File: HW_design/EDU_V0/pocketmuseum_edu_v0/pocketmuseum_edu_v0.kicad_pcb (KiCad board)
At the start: 4 copper layers, 89 x 51 mm, 141 parts, among them J101 USB_C_Receptacle_USB2.0_16P, J201 DM3AT-SF-PEJM5, J202 1x6P 2.54mm SMD, J203 1x6P 2.54mm SMD, J204 BM04B-SRSS-TB, J205 BM04B-SRSS-TB, J206 BM04B-SRSS-TB, J401 PJ31060-I, J402 PJ31060-I, Q201 L8050QLT1G, Q202 L8050QLT1G, Q401 BSS138LT3G, Q402 BSS138LT3G, SW201 PTS636, SW202 PTS636, U101 AMS1117-3.3, U102 AMS1117-3.3, U201 ESP32-C6-MINI-1/U, U301 LSM6DSL, U302 ICP20100, U401 ES8388

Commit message: Updated Readme
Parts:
- removed C103, C104: 22u, Capacitor_SMD:C_0603_1608Metric
- removed C306, C418, C420, C422: 1u, Capacitor_SMD:C_0402_1005Metric
- removed C307, C308, C411, C415, C416, C417, C419, C421: 0u1, Capacitor_SMD:C_0402_1005Metric
- removed C410, C412, C423: 10u, Capacitor_SMD:C_0603_1608Metric
- removed C413, C414: 20p, Capacitor_SMD:C_0402_1005Metric
- removed C424, C425: 47u, Capacitor_SMD:C_0603_1608Metric
- removed D202, D203, D204, D205: LESD5D5.0CT1G, Diode_SMD:D_SOD-523
- removed D301, D302, D303, D304, D305, D306: SK6805-EC20, SK_RGB:SK68xx-EC20
- removed J202, J203: 1x6P 2.54mm SMD, Connector_PinHeader_2.54mm:PinHeader_1x06_P2.54mm_Vertical_SMD_Pin1Right
- removed J204: BM04B-SRSS-TB, Connector_JST:JST_SH_BM04B-SRSS-TB_1x04-1MP_P1.00mm_Vertical
- removed J401, J402: PJ31060-I, Connector_Audio:Jack_3.5mm_PJ31060-I_Horizontal
- removed Q201, Q202: L8050QLT1G, Package_TO_SOT_SMD:SOT-23
- removed Q401, Q402: BSS138LT3G, Package_TO_SOT_SMD:SOT-23
- removed R105, R416, R417: 10R, Resistor_SMD:R_0603_1608Metric
- removed the R206 at (180.9, 80.6)
- removed R216, R217, R218, R219, R221, R418, R419, R420: 0R, Resistor_SMD:R_0603_1608Metric
- removed R401, R409, R410: 100R, Resistor_SMD:R_0402_1005Metric
- removed R402, R411, R415: 2k, Resistor_SMD:R_0402_1005Metric
- removed R403: 4R7, Resistor_SMD:R_0402_1005Metric
- removed R404, R405, R406, R407, R408: 33R, Resistor_SMD:R_0402_1005Metric
- removed R412: 100k, Resistor_SMD:R_0402_1005Metric
- removed R413, R414, R421, R422: 1k, Resistor_SMD:R_0402_1005Metric
- removed R423, R424: 10k, Resistor_SMD:R_0402_1005Metric
- removed SW202: PTS636, Button_Switch_SMD:SW_Tactile_SPST_NO_Straight_CK_PTS636Sx25SMTRLFS
- removed U101: AMS1117-3.3, Package_TO_SOT_SMD:SOT-223-3_TabPin2
- removed U401: ES8388, Package_DFN_QFN:QFN-28-1EP_4x4mm_P0.45mm_EP2.6x2.6mm
- added D2: LESD5D5.0CT1G, Diode_SMD:D_SOD-523, F.Cu at (110.0, 169.7)
- added D4: LESD5D5.0CT1G, Diode_SMD:D_SOD-523, F.Cu at (110.0, 172.2)
- added D401: SK6805-EC20, SK_RGB:SK68xx-EC20, B.Cu at (166.1, 104.8)
- added D402: SK6805-EC20, SK_RGB:SK68xx-EC20, B.Cu at (150.8, 104.8)
- added D403: SK6805-EC20, SK_RGB:SK68xx-EC20, B.Cu at (135.3, 104.6)
- added D404: SK6805-EC20, SK_RGB:SK68xx-EC20, B.Cu at (180.8, 104.8)
- added D405: SK6805-EC20, SK_RGB:SK68xx-EC20, B.Cu at (166.2, 90.0)
- added D406: SK6805-EC20, SK_RGB:SK68xx-EC20, B.Cu at (150.8, 89.8)
- added D407: SK6805-EC20, SK_RGB:SK68xx-EC20, B.Cu at (127.7, 78.0)
- added D408: SK6805-EC20, SK_RGB:SK68xx-EC20, B.Cu at (127.7, 91.8)
- added D409: SK6805-EC20, SK_RGB:SK68xx-EC20, B.Cu at (114.0, 91.8)
- added J102: JST PH S2B, Connector_JST:JST_PH_S2B-PH-SM4-TB_1x02-1MP_P2.00mm_Horizontal, F.Cu at (135.8, 76.8)
- added Q301: BSS138, Package_TO_SOT_SMD:SOT-23, F.Cu at (81.0, 99.8)
- added Q302: BSS138, Package_TO_SOT_SMD:SOT-23, F.Cu at (81.0, 104.4)
- added Q303: BSS138, Package_TO_SOT_SMD:SOT-23, F.Cu at (81.0, 109.0)
- added R303: 4k7, Resistor_SMD:R_0603_1608Metric, F.Cu at (99.9, 150.6)
- added R304: 4k7, Resistor_SMD:R_0603_1608Metric, F.Cu at (99.9, 153.1)
- added R305: 10k, Resistor_SMD:R_0603_1608Metric, F.Cu at (99.9, 155.6)
- added R306: 0R, Resistor_SMD:R_0603_1608Metric, F.Cu at (99.9, 158.1)
- added R307: 0R, Resistor_SMD:R_0603_1608Metric, F.Cu at (99.9, 160.6)
- added SW1: SW_SPDT, Button_Switch_SMD:SW_SPDT_PCM12, F.Cu at (123.5, 67.6)
- added U1: TLV740P18, Package_TO_SOT_SMD:SOT-23-5, F.Cu at (93.4, 133.8)
- added U302: ICP20100, Package_LGA:ST_HLGA-10_2x2mm_P0.5mm_LayoutBorder3x2y, F.Cu at (103.8, 160.0)
- C204: moved to F.Cu
- C301, C302, C303, C304, C305: value 1u -> 0u1; moved to F.Cu
- C401, C403, C405, C408: value 10u -> 1u; footprint Capacitor_SMD:C_0603_1608Metric -> Capacitor_SMD:C_0402_1005Metric
- C402, C404, C406, C407, C409: value 0u1 -> 1u
- D201: value LESD5D5.0CT1G -> LED; footprint Diode_SMD:D_SOD-523 -> LED_SMD:LED_0402_1005Metric
- J201: value DM3AT-SF-PEJM5 -> TF-015; footprint Connector_Card:microSD_HC_Hirose_DM3AT-SF-PEJM5 -> microSD:TF-015_SOFNG
- J205, J206: footprint Connector_JST:JST_SH_BM04B-SRSS-TB_1x04-1MP_P1.00mm_Vertical -> Connector_JST:JST_SH_SM04B-SRSS-TB_1x04-1MP_P1.00mm_Horizontal
- R208: value 10k -> 0R; footprint Resistor_SMD:R_0402_1005Metric -> Resistor_SMD:R_0603_1608Metric
- R214: value 0R -> 10k; footprint Resistor_SMD:R_0603_1608Metric -> Resistor_SMD:R_0402_1005Metric
- R215: value 0R -> 2k; footprint Resistor_SMD:R_0603_1608Metric -> Resistor_SMD:R_0402_1005Metric
- R301, R302: value 0R -> 10k; moved to F.Cu
- R303, R304: value 0R -> 4k7
- U301: value LSM6DSL -> ICM-20948; footprint Package_LGA:LGA-14_3x2.5mm_P0.5mm_LayoutBorder3x4y -> Sensor_Motion:InvenSense_QFN-24_3x3mm_P0.4mm
- moved D102 111.6 mm to (202.0, 149.3)
- moved D101 111.6 mm to (202.0, 143.0)
- moved R102 111.6 mm to (196.5, 140.3)
- moved R101 111.6 mm to (196.5, 151.9)
- moved C304 85.3 mm to (108.3, 151.2)
- moved C303 84.0 mm to (108.3, 149.2), turned to 0 degrees
- moved C401 73.4 mm to (76.8, 137.4), turned to 0 degrees
- moved C402 72.6 mm to (76.8, 139.3), turned to 0 degrees
- moved C305 72.2 mm to (108.3, 153.2)
- moved C403 69.6 mm to (76.8, 141.3)
- moved R302 68.9 mm to (99.9, 148.1), turned to 0 degrees
- moved C408 68.6 mm to (82.5, 139.3), turned to 0 degrees
- moved R301 68.6 mm to (99.9, 145.6)
- moved J101 67.6 mm to (165.6, 112.7), turned to 0 degrees
- moved C302 66.8 mm to (108.3, 147.2), turned to 0 degrees
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- renumbered R207 to R206, R220 to R207
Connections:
- net Net-(J101-CC1) renamed /Power/USB_CC1
- net Net-(J101-CC2) renamed /Power/USB_CC2
- C204 pad 1: /MCU/CHIP_PU -> GND
- C204 pad 2: GND -> /MCU/CHIP_PU
- C301 pad 1: GND -> +1.8V
- C301 pad 2: +3.3V -> GND
- C302 pad 2: +3.3V -> +1.8V
- C303 pad 2: +3.3V -> Net-(U301-REGOUT)
- C304 pad 1: GND -> +3.3V
- C304 pad 2: +3.3V -> GND
- C401 pad 1: +3.3V -> GND
- C401 pad 2: GND -> +3.3V
- C402 pad 1: /Audio CODEC/ES8388_DVDD -> GND
- C402 pad 2: GND -> +3.3V
- C403 pad 1: +3.3VA -> GND
- C403 pad 2: GND -> +3.3V
- C404 pad 1: +3.3VA -> GND
- C404 pad 2: GND -> +3.3V
- C405 pad 1: /Audio CODEC/ES8388_AVDD -> GND
- C405 pad 2: GND -> +3.3V
- C406 pad 1: /Audio CODEC/ES8388_AVDD -> GND
- C406 pad 2: GND -> +3.3V
- C407 pad 1: /Audio CODEC/ES8388_VREF -> GND
- C407 pad 2: GND -> +3.3V
- C408 pad 1: /Audio CODEC/ES8388_VREF -> GND
- C408 pad 2: GND -> +3.3V
- C409 pad 1: /Audio CODEC/ES8388_ADCVREF -> GND
- C409 pad 2: GND -> +3.3V
- D201 pad 2: /MCU/FTDI_DTR -> Net-(D201-A)
- J101 pad A6: unconnected-(J101-D+-PadA6) -> USB_D+
- J101 pad A7: unconnected-(J101-D--PadA7) -> USB_D-
- J101 pad B6: unconnected-(J101-D+-PadB6) -> USB_D+
- J101 pad B7: unconnected-(J101-D--PadB7) -> USB_D-
- J101 pad S1: /Power/USB_shield_disconnect -> unconnected-(J101-SHIELD-PadS1)_2
- J201 pad 1: /MCU/uSD_DAT2 -> /MCU/SD_DAT2
- J201 pad 10: /MCU/SD_DETECT -> /MCU/SD_Shield_Diconnect
- J201 pad 2: /MCU/uSD_DAT3 -> /MCU/SPI_CS
- J201 pad 3: /MCU/uSD_CMD -> /MCU/SPI_MOSI
- J201 pad 5: /MCU/uSD_CLK -> /MCU/SPI_SCK
- J201 pad 7: /MCU/uSD_DAT0 -> /MCU/SPI_MISO
- J201 pad 8: /MCU/uSD_DAT1 -> /MCU/SD_DAT1
- J201 pad 9: +3.3V -> /MCU/SD_DETECT
- J205 pad MP: unconnected-(J205-MountPin-PadMP)_1 -> /MCU/unconnected-(J205-MountPin-PadMP)_1
- J206 pad 2: /MCU/STRAP_GPIO8 -> /MCU/CHIP_PU
- J206 pad 3: /MCU/SD_DETECT -> /MCU/UART0_RX
- J206 pad 4: /MCU/MCU_GPIO14 -> /MCU/UART0_TX
- J206 pad MP: unconnected-(J206-MountPin-PadMP) -> /MCU/unconnected-(J206-MountPin-PadMP)_1_1
- R205 pad 1: /MCU/FTDI_DTR -> +3.3V
- R205 pad 2: /MCU/DTR -> /MCU/STRAP_GPIO_9
- R207 pad 2: GND -> +3.3V
- R208 pad 1: /MCU/uSD_DAT1 -> /MCU/SD_Shield_Diconnect
- R208 pad 2: +3.3V -> GND
- R209 pad 1: /MCU/uSD_DAT0 -> /MCU/SPI_MISO
- R210 pad 1: /MCU/uSD_CLK -> /MCU/SPI_SCK
- R211 pad 1: /MCU/uSD_CMD -> /MCU/SPI_MOSI
- R212 pad 1: /MCU/uSD_DAT3 -> /MCU/SPI_CS
- R213 pad 1: /MCU/uSD_DAT2 -> /MCU/SD_DAT1
- R214 pad 1: /MCU/uSD_DAT2 -> /MCU/SD_DAT2
- R214 pad 2: /MCU/SDIO_DAT2 -> +3.3V
- R215 pad 1: /MCU/uSD_DAT3 -> /MCU/DBG_LED
- R215 pad 2: /MCU/SDIO_DAT3 -> Net-(D201-A)
- R301 pad 1: Net-(U301-SDA) -> +1.8V
- R301 pad 2: I2C_SDA -> /Sensors/ICM20x_SCL
- R302 pad 1: Net-(U301-SCL) -> +1.8V
- R302 pad 2: I2C_SCL -> /Sensors/ICM20x_SDA
- R303 pad 1: Net-(U302-SCL) -> +3.3V
- R304 pad 1: Net-(U302-SDA) -> +1.8V
- R304 pad 2: I2C_SDA -> /Sensors/ICM20x_INT
- U201 pad 10: /MCU/STRAP_MTDI -> unconnected-(U201-MTDI/GPIO5/ADC1_CH5-Pad10)
- U201 pad 12: I2S_DOUT -> unconnected-(U201-GPIO0/ADC1_CH0/XTAL_32K_P-Pad12)
- U201 pad 13: I2S_LRCK -> unconnected-(U201-GPIO1/ADC1_CH1/XTAL_32K_N-Pad13)
- U201 pad 15: I2S_DIN -> unconnected-(U201-MTCK/GPIO6/ADC1_CH6-Pad15)
- U201 pad 16: I2S_BCK -> /MCU/DBG_LED
- U201 pad 17: I2S_MCLK -> USB_D-
- U201 pad 18: AUX_IN_DETECT -> USB_D+
- U201 pad 19: /MCU/MCU_GPIO14 -> unconnected-(U201-GPIO14-Pad19)
- U201 pad 24: /MCU/SDIO_CMD -> /MCU/SPI_MOSI
- U201 pad 25: /MCU/SDIO_CLK -> /MCU/SPI_SCK
- U201 pad 26: /MCU/SDIO_DAT0 -> /MCU/SPI_MISO
- U201 pad 27: /MCU/SDIO_DAT1 -> unconnected-(U201-GPIO21-Pad27)
- U201 pad 28: /MCU/SDIO_DAT2 -> unconnected-(U201-GPIO22-Pad28)
- U201 pad 29: /MCU/SDIO_DAT3 -> /MCU/SPI_CS
- U201 pad 9: /MCU/STRAP_MTMS -> unconnected-(U201-MTMS/GPIO4/ADC1_CH4-Pad9)
- U301 pad 1: GND -> unconnected-(U301-NC-Pad1)
- U301 pad 10: unconnected-(U301-NC-Pad10) -> Net-(U301-REGOUT)
- U301 pad 12: +3.3V -> /Sensors/ICM20x_INT
- U301 pad 13: Net-(U301-SCL) -> +1.8V
- U301 pad 14: Net-(U301-SDA) -> unconnected-(U301-NC-Pad14)
- U301 pad 2: GND -> unconnected-(U301-NC-Pad2)
- U301 pad 3: GND -> unconnected-(U301-NC-Pad3)
- U301 pad 5: +3.3V -> unconnected-(U301-NC-Pad5)
- U301 pad 6: GND -> unconnected-(U301-NC-Pad6)
- U301 pad 7: GND -> unconnected-(U301-AUX_CL-Pad7)
- U301 pad 8: +3.3V -> +1.8V
- U301 pad 9: unconnected-(U301-INT2-Pad9) -> GND
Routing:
- net +3.3V: track 287.9 -> 0.00 mm, vias 13 -> 0
- net GND: track 115.8 -> 0.00 mm, vias 142 -> 0
- net VBUS: track 103.4 -> 0.00 mm, vias 2 -> 0
- net I2C_SCL: track 82.4 -> 0.00 mm, vias 1 -> 0
- net I2C_SDA: track 65.7 -> 0.00 mm, vias 1 -> 0
- net /Audio CODEC/AUX_Det: track 60.7 -> 0.00 mm
- net /MCU/SD_DETECT: track 52.4 -> 0.00 mm
- net +3.3VA: track 44.6 -> 0.00 mm
- net AUX_IN_DETECT: track 41.2 -> 0.00 mm
- net ES8388_I2S_MCLK: track 40.0 -> 0.00 mm
- net ES8388_I2S_BCK: track 34.3 -> 0.00 mm
- net ES8388_I2S_DIN: track 32.3 -> 0.00 mm
- net ES8388_I2S_LRCK: track 30.3 -> 0.00 mm
- net I2S_DOUT: track 28.6 -> 0.00 mm
- net /MCU/CHIP_PU: track 27.9 -> 0.00 mm, vias 2 -> 0
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- removed copper zone on B.Cu, net +3.3V
- removed copper zone on F.Cu, net +3.3V
- removed copper zone on F.Cu, net +3.3VA
- removed copper zone on F.Cu, net +5V
- removed copper zone on F.Cu, net /Audio CODEC/AUX_VREF
- removed copper zone on F.Cu, net /Audio CODEC/ES8388_DVDD
- removed copper zone on F.Cu, net /MCU/CHIP_PU
- removed copper zone on F.Cu, net /Power/5V_Filt_A
- removed copper zone on F.Cu, net /Power/5V_Filt_D
- removed copper zone on B.Cu, net GND
- removed copper zone on F.Cu, net GND
- removed copper zone on In1.Cu, net GND
- removed copper zone on In2.Cu, net GND
- removed copper zone on F.Cu, net VBUS
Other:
- board size 89 x 51 mm -> 92.1 x 51 mm
- board text removed: "14"
- board text removed: "9"
- board text removed: "AUX IN"
- board text removed: "BARO."
- board text removed: "FTDI"
- board text removed: "GPIO"
- board text removed: "I2C"
- board text removed: "I2S"
- board text removed: "IMU"
- board text removed: "MTx & VA"
- board text removed: "PHONES OUT"
- board text removed: "PWR IN"
- board text removed: "SD CARD"
- board text removed: "SOUNCARD DEV. V0"
- board text removed: "_2_"
- board text removed: "_3_"
- board text removed: "_4_"
- board text removed: "_5_"
- board text removed: "_gpio9"
- board text removed: "_reset"

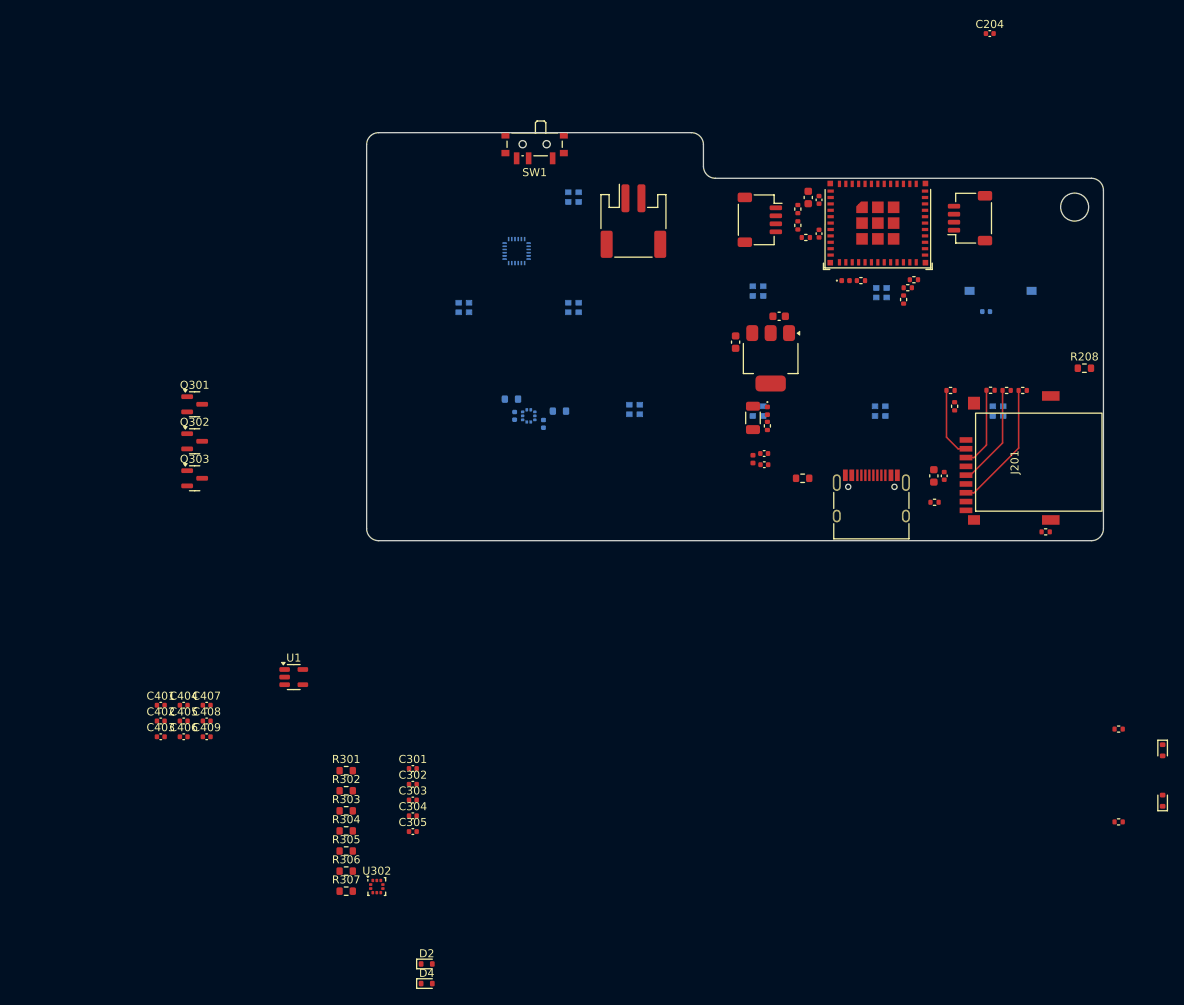
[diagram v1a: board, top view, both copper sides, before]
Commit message: Added Mic & Light Sensor to EDU_V0
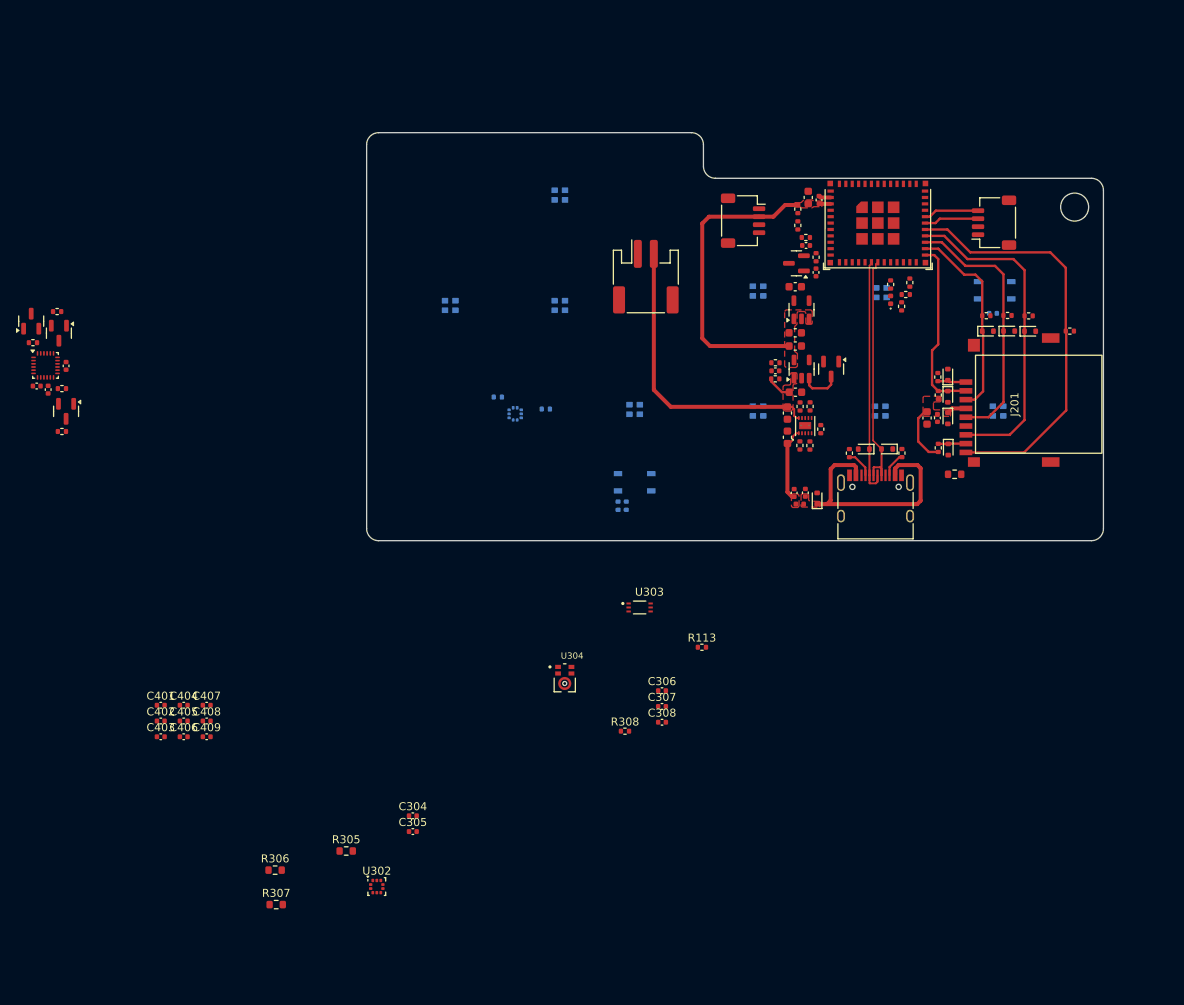
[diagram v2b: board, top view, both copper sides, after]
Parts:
- removed the C106 at (154.1, 88.8)
- removed C205: 1u, Capacitor_SMD:C_0402_1005Metric
- removed C309, C310: 0u1, Capacitor_SMD:C_0402_1005Metric
- removed D2, D4: LESD5D5.0CT1G, Diode_SMD:D_SOD-523
- removed SW1: SW_SPDT, Button_Switch_SMD:SW_SPDT_PCM12
- removed U1: TLV740P18, Package_TO_SOT_SMD:SOT-23-5
- added C103: 10u, Capacitor_SMD:C_0603_1608Metric, F.Cu at (155.1, 103.9)
- added C104: 10u, Capacitor_SMD:C_0603_1608Metric, F.Cu at (155.1, 100.8)
- added C105: 1u, Capacitor_SMD:C_0402_1005Metric, F.Cu at (153.6, 95.6)
- added C107: 10u, Capacitor_SMD:C_0603_1608Metric, F.Cu at (156.1, 98.2)
- added C108: 10u, Capacitor_SMD:C_0603_1608Metric, F.Cu at (156.1, 92.5)
- added C109: 10u, Capacitor_SMD:C_0603_1608Metric, F.Cu at (156.1, 90.8)
- added C110: 10u, Capacitor_SMD:C_0603_1608Metric, F.Cu at (156.1, 85.1)
- added C306: 0u1, Capacitor_SMD:C_0402_1005Metric, F.Cu at (139.4, 135.6)
- added C307: 1u, Capacitor_SMD:C_0402_1005Metric, F.Cu at (139.4, 137.5)
- added C308: 0u1, Capacitor_SMD:C_0402_1005Metric, F.Cu at (139.4, 139.5)
- added D104: BAT54C, Package_TO_SOT_SMD:SOT-23, F.Cu at (160.6, 95.3)
- added D202: LESD5D5.0CT1G, Diode_SMD:D_SOD-523, F.Cu at (185.4, 90.6)
- added D203: LESD5D5.0CT1G, Diode_SMD:D_SOD-523, F.Cu at (182.8, 90.6)
- added D204: LESD5D5.0CT1G, Diode_SMD:D_SOD-523, F.Cu at (175.2, 101.5)
- added D205: LESD5D5.0CT1G, Diode_SMD:D_SOD-523, F.Cu at (180.2, 90.6)
- added D206: LESD5D5.0CT1G, Diode_SMD:D_SOD-523, F.Cu at (175.2, 98.8)
- added D207: LESD5D5.0CT1G, Diode_SMD:D_SOD-523, F.Cu at (175.2, 96.0)
- added D208: LED, LED_SMD:LED_0402_1005Metric, F.Cu at (168.0, 86.7)
- added R105: 10k, Resistor_SMD:R_0402_1005Metric, F.Cu at (156.7, 100.0)
- added R107: 10k, Resistor_SMD:R_0402_1005Metric, F.Cu at (159.3, 102.9)
- added R108: 61k9, Resistor_SMD:R_0402_1005Metric, F.Cu at (153.6, 94.6)
- added R109: 178k, Resistor_SMD:R_0402_1005Metric, F.Cu at (153.6, 96.6)
- added R110: 100k, Resistor_SMD:R_0402_1005Metric, F.Cu at (158.7, 81.4)
- added R111: 2k7, Resistor_SMD:R_0402_1005Metric, B.Cu at (133.9, 112.4)
- added R112: 10k, Resistor_SMD:R_0402_1005Metric, B.Cu at (134.9, 112.4)
- added R113: 10k, Resistor_SMD:R_0402_1005Metric, F.Cu at (144.4, 130.1)
- added R308: 1k, Resistor_SMD:R_0402_1005Metric, F.Cu at (134.8, 140.6)
- added SW101: PTS810SJG250, Button_Switch_SMD:SW_SPST_PTS810, B.Cu at (136.0, 109.5)
- added U101: BQ24040, DFNCustom:QFN-10_EP_2.1x2.1_Pitch0.4mm, F.Cu at (157.3, 102.4)
- added U103: AP2112K-3.3, Package_TO_SOT_SMD:SOT-23-5, F.Cu at (156.9, 95.3)
- added U104: AP2112K-1.8, Package_TO_SOT_SMD:SOT-23-5, F.Cu at (156.9, 87.9)
- added U303: BH1750FVI, WSOF:XDCR_BH1750FVI-TR, F.Cu at (136.6, 125.2)
- added U304: T3902, MMICT:MMIC, F.Cu at (127.3, 133.9)
- C106: renamed from C105; value 47u -> 0u1; footprint Capacitor_SMD:C_0603_1608Metric -> Capacitor_SMD:C_0402_1005Metric
- C204: value 0u1 -> 1u
- D103, D201: value LED -> LESD5D5.0CT1G; footprint LED_SMD:LED_0402_1005Metric -> Diode_SMD:D_SOD-523
- R103: value 0R -> 1k2; footprint Resistor_SMD:R_0603_1608Metric -> Resistor_SMD:R_0402_1005Metric
- R104: value 2k -> 6k8
- R106: value 2R2 -> 10k; footprint Resistor_SMD:R_1206_3216Metric -> Resistor_SMD:R_0402_1005Metric
- R301, R302: value 10k -> 5k1; footprint Resistor_SMD:R_0603_1608Metric -> Resistor_SMD:R_0402_1005Metric
- R303 (x2), R304 (x2): footprint Resistor_SMD:R_0603_1608Metric -> Resistor_SMD:R_0402_1005Metric
- SW201: value PTS636 -> PTS810SJG250; footprint Button_Switch_SMD:SW_Tactile_SPST_NO_Straight_CK_PTS636Sx25SMTRLFS -> Button_Switch_SMD:SW_SPST_PTS810
- U102: value AMS1117-3.3 -> APX803-29SAG; footprint Package_TO_SOT_SMD:SOT-223-3_TabPin2 -> Package_TO_SOT_SMD:SOT-23
- U301: moved to F.Cu
- moved C303 68.6 mm to (62.7, 97.9), turned to 90 degrees
- moved R302 68.3 mm to (60.8, 92.0)
- moved C302 67.9 mm to (64.9, 95.0), turned to -90 degrees
- moved R301 67.8 mm to (63.8, 88.2), turned to 180 degrees
- moved C301 67.1 mm to (61.3, 97.5)
- moved R304 65.7 mm to (64.4, 97.8), turned to 180 degrees
- moved U301 60.6 mm to (62.4, 94.9), turned to 0 degrees
- moved R303 59.3 mm to (64.4, 103.2)
- moved D102 57.7 mm to (164.7, 105.3), turned to 180 degrees
- moved R101 53.5 mm to (169.4, 105.8), turned to 90 degrees
- moved D101 53.4 mm to (158.8, 111.5), turned to 90 degrees
- moved R102 48.2 mm to (162.8, 105.9), turned to 90 degrees
- moved C204 35.1 mm to (157.4, 79.9), turned to 180 degrees
- moved R207 25.3 mm to (190.4, 90.6)
- moved D201 24.7 mm to (175.2, 105.4), turned to -90 degrees
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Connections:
- net +1.8V renamed +1V8
- C101 pad 1: VBUS -> VUSB
- C106 pad 1: /Power/5V_Filt_D -> +3V3
- C201 pad 1: +3.3V -> +3V3
- C202 pad 1: +3.3V -> +3V3
- C204 pad 1: GND -> CHIP_PU
- C204 pad 2: /MCU/CHIP_PU -> GND
- C206 pad 1: +3.3V -> +3V3
- C207 pad 1: +3.3V -> +3V3
- C304 pad 1: +3.3V -> +3V3
- C305 pad 2: +3.3V -> +3V3
- C401 pad 2: +3.3V -> +3V3
- C402 pad 2: +3.3V -> +3V3
- C403 pad 2: +3.3V -> +3V3
- C404 pad 2: +3.3V -> +3V3
- C405 pad 2: +3.3V -> +3V3
- C406 pad 2: +3.3V -> +3V3
- C407 pad 2: +3.3V -> +3V3
- C408 pad 2: +3.3V -> +3V3
- C409 pad 2: +3.3V -> +3V3
- D101 pad 1: GND -> VUSB
- D101 pad 2: VBUS -> GND
- D102 pad 1: GND -> USB_D-
- D102 pad 2: VBUS -> GND
- D103 pad 2: Net-(D103-A) -> USB_D+
- D201 pad 1: GND -> /MCU/SD_DAT1
- D201 pad 2: Net-(D201-A) -> GND
- D401 pad 1: +3.3V -> +3V3
- D402 pad 1: +3.3V -> +3V3
- D403 pad 1: +3.3V -> +3V3
- D404 pad 1: +3.3V -> +3V3
- D405 pad 1: +3.3V -> +3V3
- D406 pad 1: +3.3V -> +3V3
- D407 pad 1: +3.3V -> +3V3
- D408 pad 1: +3.3V -> +3V3
- D409 pad 1: +3.3V -> +3V3
- J101 pad B4: VBUS -> VUSB
- J101 pad B9: VBUS -> VUSB
- J102 pad 1: unconnected-(J102-Pin_1-Pad1) -> GND
- J102 pad 2: unconnected-(J102-Pin_2-Pad2) -> VBAT_ALW_ON
- J201 pad 4: +3.3V -> +3V3
- J205 pad 2: +3.3V -> +3V3
- J205 pad MP: /MCU/unconnected-(J205-MountPin-PadMP)_1 -> unconnected-(J205-MountPin-PadMP)
- J206 pad 2: /MCU/CHIP_PU -> CHIP_PU
- J206 pad MP: /MCU/unconnected-(J206-MountPin-PadMP)_1_1 -> unconnected-(J206-MountPin-PadMP)_1
- L101 pad 1: VBUS -> VUSB
- Q303 pad 3: I2C_SCL -> MEMS_INT
- R103 pad 1: /Power/USB_shield_disconnect -> GND
- R103 pad 2: GND -> /Power/BQ2404_ISET
- R104 pad 1: +5V -> GND
- R104 pad 2: Net-(D103-A) -> /Power/BQ2404_PRE_TERM
- R106 pad 1: +5V -> +3V3
- R106 pad 2: /Power/5V_Filt_D -> BATT_CHRG_FDBCK
- R201 pad 1: +3.3V -> +3V3
- R202 pad 1: +3.3V -> +3V3
- R204 pad 2: +3.3V -> +3V3
- R205 pad 1: +3.3V -> +3V3
- R206 pad 1: /MCU/CHIP_PU -> CHIP_PU
- R206 pad 2: +3.3V -> +3V3
- R207 pad 2: +3.3V -> +3V3
- R209 pad 1: /MCU/SPI_MISO -> /MCU/SD_DAT1
- R209 pad 2: +3.3V -> +3V3
- R210 pad 1: /MCU/SPI_SCK -> /MCU/SPI_MISO
- R210 pad 2: +3.3V -> +3V3
- R211 pad 1: /MCU/SPI_MOSI -> /MCU/SPI_SCK
- R211 pad 2: +3.3V -> +3V3
- R212 pad 1: /MCU/SPI_CS -> /MCU/SPI_MOSI
- R212 pad 2: +3.3V -> +3V3
- R213 pad 1: /MCU/SD_DAT1 -> /MCU/SPI_CS
- R213 pad 2: +3.3V -> +3V3
- R214 pad 2: +3.3V -> +3V3
- R215 pad 2: Net-(D201-A) -> Net-(D208-A)
- R303 pad 1: +3.3V -> +3V3 (x2)
- R303 pad 2: I2C_SCL -> MEMS_INT (x2)
- U102 pad 2: +3.3V -> CHIP_PU
- U102 pad 3: /Power/5V_Filt_D -> +3V3
- U201 pad 10: unconnected-(U201-MTDI/GPIO5/ADC1_CH5-Pad10) -> BATT_POWOK_FDBCK
- U201 pad 12: unconnected-(U201-GPIO0/ADC1_CH0/XTAL_32K_P-Pad12) -> BATT_VOLT_FDBCK
- U201 pad 13: unconnected-(U201-GPIO1/ADC1_CH1/XTAL_32K_N-Pad13) -> BATT_SW_FDBCK
- U201 pad 15: unconnected-(U201-MTCK/GPIO6/ADC1_CH6-Pad15) -> BATT_ATTCH_CMD
- U201 pad 16: /MCU/DBG_LED -> MEMS_INT
- U201 pad 19: unconnected-(U201-GPIO14-Pad19) -> I2S_CLK
- U201 pad 20: /MCU/SD_DETECT -> /MCU/DBG_LED
- U201 pad 24: /MCU/SPI_MOSI -> I2S_DAT
- U201 pad 25: /MCU/SPI_SCK -> /MCU/SPI_CS
- U201 pad 26: /MCU/SPI_MISO -> /MCU/SPI_MOSI
- U201 pad 27: unconnected-(U201-GPIO21-Pad27) -> /MCU/SPI_SCK
- U201 pad 28: unconnected-(U201-GPIO22-Pad28) -> /MCU/SPI_MISO
- U201 pad 29: /MCU/SPI_CS -> /MCU/SD_DETECT
- U201 pad 3: +3.3V -> +3V3
- U201 pad 8: /MCU/CHIP_PU -> CHIP_PU
- U201 pad 9: unconnected-(U201-MTMS/GPIO4/ADC1_CH4-Pad9) -> BATT_CHRG_FDBCK
- U302 pad 1: +3.3V -> +3V3 (x2)
- U302 pad 10: +3.3V -> +3V3 (x2)
- U302 pad 5: +3.3V -> +3V3 (x2)
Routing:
- net /MCU/SD_DETECT: track 0.00 -> 52.1 mm
- net +3V3: track 0.00 -> 49.8 mm
- net VBAT_ALW_ON: track 0.00 -> 40.2 mm
- net VUSB: track 0.00 -> 30.6 mm
- net USB_D+: track 0.00 -> 30.4 mm
- net USB_D-: track 0.00 -> 29.6 mm
- net /MCU/SPI_MISO: track 16.1 -> 41.0 mm
- net /MCU/SPI_SCK: track 12.8 -> 32.9 mm
- net /MCU/SPI_MOSI: track 10.1 -> 25.2 mm
- net /MCU/SPI_CS: track 8.89 -> 22.5 mm
- net +5V: track 0.00 -> 9.37 mm
- net /MCU/UART0_TX: track 0.00 -> 6.94 mm
- net /MCU/UART0_RX: track 0.00 -> 6.85 mm
- net /Power/3V3_LDO_EN: track 0.00 -> 4.98 mm
- net /MCU/SD_DAT2: track 0.00 -> 3.65 mm
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- added copper zone on F.Cu, net +3V3
- added copper zone on F.Cu, net +5V
- added copper zone on F.Cu, net VBAT_ALW_ON
- added copper zone on F.Cu, net VUSB

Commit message: Diagram review complete
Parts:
- removed D201, D202, D203, D204, D205, D206, D207: LESD5D5.0CT1G, Diode_SMD:D_SOD-523
- removed the R303 at (118.9, 98.9)
- removed the R304 at (124.9, 100.4)
- removed the U302 at (121.1, 101.0)
- added R114: 0R, Resistor_SMD:R_0603_1608Metric, F.Cu at (173.3, 113.7)
- C301: value 0u1 -> 1u; moved to B.Cu
- C302, C303, C304, C305, C306, C307, Q301, Q302, Q303, R301, R302, R308, U301, U302, U303: moved to B.Cu
- R111: value 2k7 -> 3k3
- R303: value 4k7 -> 5k1
- R304: value 4k7 -> 5k1; moved to B.Cu
- R305: footprint Resistor_SMD:R_0603_1608Metric -> Resistor_SMD:R_0402_1005Metric; moved to B.Cu
- U101: footprint DFNCustom:QFN-10_EP_2.1x2.1_Pitch0.4mm -> DFNCustom:QFN_10_BQ24040
- moved R303 102.2 mm to (164.9, 84.3), turned to 90 degrees
- moved Q301 71.6 mm to (129.4, 108.8)
- moved R302 71.3 mm to (129.4, 111.3), turned to 180 degrees
- moved U302 69.4 mm to (127.2, 94.7), turned to -90 degrees
- moved R301 68.5 mm to (130.2, 105.2), turned to -90 degrees
- moved C301 67.3 mm to (127.1, 111.8), turned to 180 degrees
- moved C308 65.1 mm to (132.0, 74.9), turned to 90 degrees
- moved U301 64.8 mm to (125.6, 109.0), turned to 180 degrees
- moved C303 64.6 mm to (125.6, 112.3)
- moved Q302 64.1 mm to (126.6, 105.2), turned to 180 degrees
- moved C305 61.0 mm to (129.0, 95.8), turned to 90 degrees
- moved C302 59.8 mm to (123.1, 108.9)
- moved Q303 59.5 mm to (123.1, 113.1), turned to 0 degrees
- moved U304 59.5 mm to (129.4, 74.5), turned to -90 degrees
- moved C304 59.0 mm to (125.5, 94.8), turned to -90 degrees
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- renumbered C404 to C401, C405 to C402, C401 to C403, C402 to C404, C403 to C405, D404 to D401, D405 to D402, D401 to D403, D402 to D404, D403 to D405
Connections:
- D401 pad 2: /Feedback/WS2812B_Chain4 -> /Feedback/WS2812B_Chain1
- D401 pad 4: /Feedback/WS2812B_Chain3 -> WS2812B_D
- D402 pad 2: /Feedback/WS2812B_Chain5 -> /Feedback/WS2812B_Chain2
- D402 pad 4: /Feedback/WS2812B_Chain4 -> /Feedback/WS2812B_Chain1
- D403 pad 2: /Feedback/WS2812B_Chain1 -> /Feedback/WS2812B_Chain3
- D403 pad 4: WS2812B_D -> /Feedback/WS2812B_Chain2
- D404 pad 2: /Feedback/WS2812B_Chain2 -> /Feedback/WS2812B_Chain4
- D404 pad 4: /Feedback/WS2812B_Chain1 -> /Feedback/WS2812B_Chain3
- D405 pad 2: /Feedback/WS2812B_Chain3 -> /Feedback/WS2812B_Chain5
- D405 pad 4: /Feedback/WS2812B_Chain2 -> /Feedback/WS2812B_Chain4
- J101 pad S1: unconnected-(J101-SHIELD-PadS1)_2 -> Net-(J101-SHIELD)
- J102 pad 1: GND -> VBAT_ALW_ON
- J102 pad 2: VBAT_ALW_ON -> GND
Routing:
- net BATT_POWOK_FDBCK: track 0.00 -> 31.2 mm, vias 0 -> 2
- net BATT_CHRG_FDBCK: track 0.00 -> 30.6 mm, vias 0 -> 2
- net +3V3: track 49.8 -> 80.0 mm, vias 0 -> 2
- net CHIP_PU: track 0.00 -> 29.7 mm, vias 0 -> 2
- net /MCU/STRAP_GPIO_9: track 0.00 -> 23.3 mm, vias 0 -> 2
- net GND: track 1.52 -> 22.9 mm, vias 0 -> 27
- net BATT_VOLT_FDBCK: track 0.00 -> 19.5 mm, vias 0 -> 2
- net BATT_ATTCH_CMD: track 0.00 -> 14.2 mm
- net /Sensors/ICM20x_SDA: track 0.00 -> 5.99 mm
- net /Sensors/ICM20x_SCL: track 0.00 -> 5.54 mm
- net /Sensors/ICM20x_INT: track 0.00 -> 5.45 mm
- net +1V8: track 0.00 -> 5.40 mm
- net /MCU/STRAP_GPIO8: track 0.00 -> 5.09 mm
- net /Sensors/ICM20x_CS: track 0.00 -> 4.81 mm
- net VUSB: track 30.6 -> 34.3 mm
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- added copper zone on F.Cu, net GND
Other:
- board size 92.1 x 51 mm -> 96.8 x 51 mm
